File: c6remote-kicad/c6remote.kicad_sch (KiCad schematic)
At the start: 29 parts, among them J1 Battery, Q1 MMBT2222A, SW1 SW_Push, SW10 SW_Push, SW11 SW_Push, SW2 SW_Push, SW3 SW_Push, SW4 SW_Push, SW5 SW_Push, SW6 SW_Push, SW7 SW_Push, SW8 SW_Push, SW9 SW_Push, U1 XIAO-ESP32-C6, U2 TSOP4136, U3 PCF8575DBR

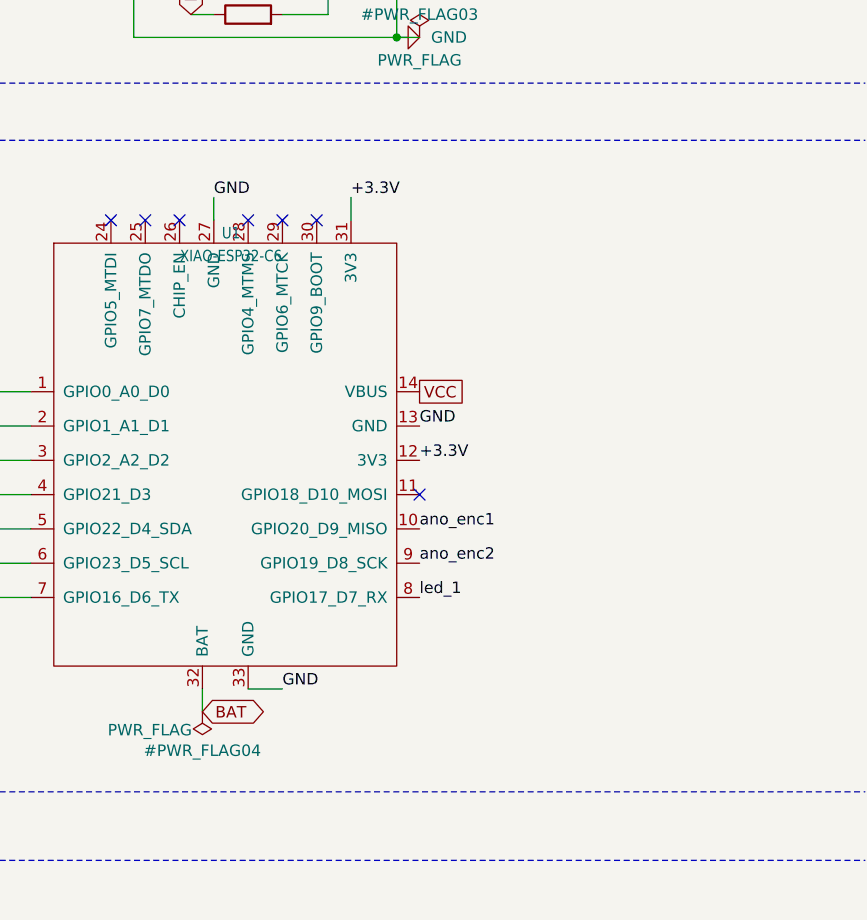
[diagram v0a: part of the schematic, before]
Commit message: feat(batt): add battery voltage-sense divider R7/R8 (100k/100k 0603) BAT->bat_sense->GND with midpoint to U1 GPIO4/pin28 ADC (halves 4.2V LiPo to ~2.1V for 3.3V ADC, ~21uA drain), routed on PCB w/ DRC 0 errors + 0 unconnected; regenerated export/ gerbers+drill+pos+BOM incl R7/R8; firmware reads ADC1 on GPIO4 as V_batt=V_adc*2. (sch/pcb reformatted by KiCad re-save, semantic delta is only the divider + routing)
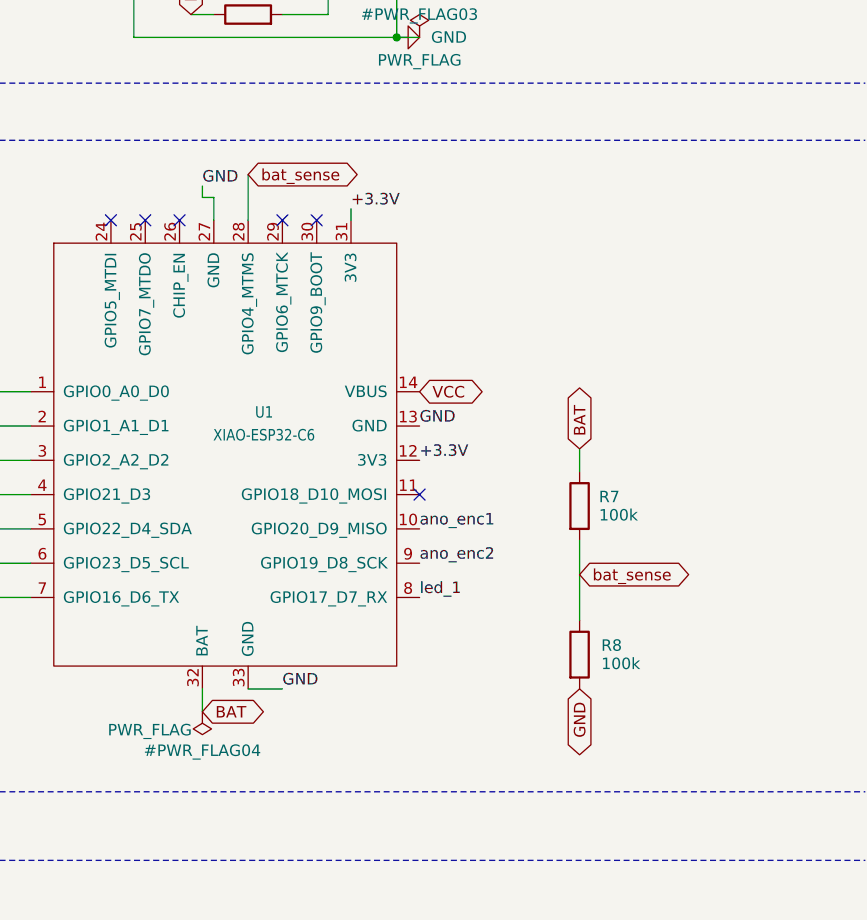
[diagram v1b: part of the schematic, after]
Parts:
- added R7, R8: 100k, Resistor_SMD:R_0603_1608Metric, symbol Device:R
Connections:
- net BAT: now also R7.1
- net GND: now also R8.2
- net bat_sense: now reaches U1.28 (GPIO4_MTMS)
- net bat_sense: now also R7.2, R8.1
- no-connect marks 9 -> 8

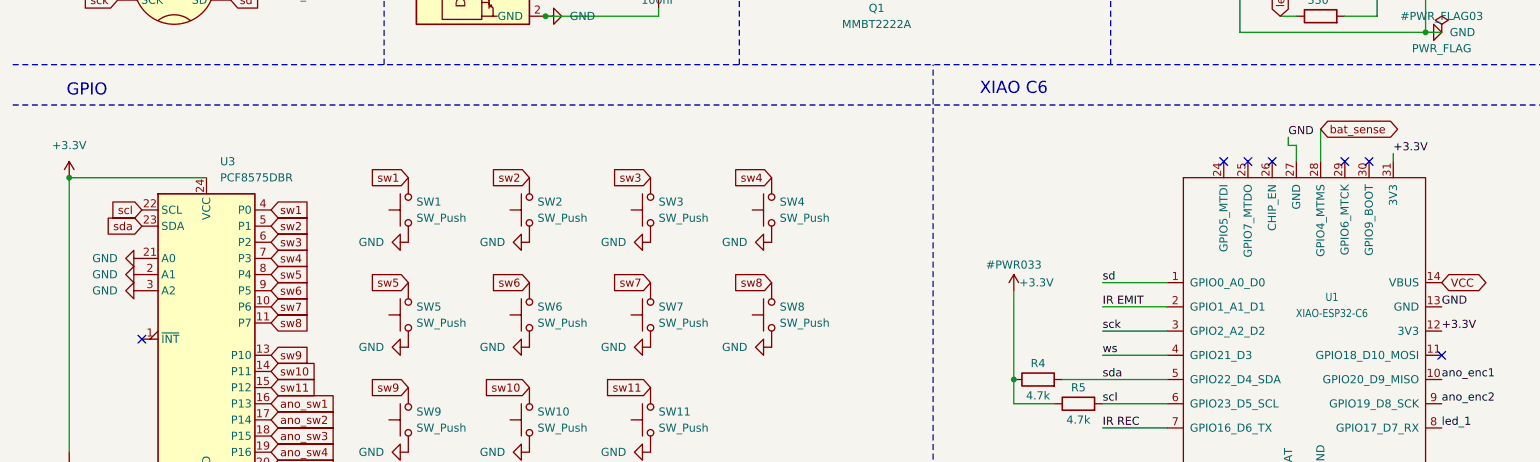
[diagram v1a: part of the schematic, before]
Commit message: feat(wake): add deep-sleep button wake via U3 PCF8575 ~INT -> new exp_int net to U1 GPIO5/pad24 (LP GPIO, ext1 wake) with R9 100k 0603 pullup to +3.3V next to R7/R8; schematic label + stale no-connect removed, board routed U3 pad1 down west channel x=48.25 w/ 2 vias joining existing GPIO5 trace at via (58.5,156.75); DRC 0 errors 0 unconnected (14 parity warns = pre-existing TP_*), no new ERC; regen export/ fab + readme renders; fw: esp_sleep_enable_ext1_wakeup(BIT(5), ANY_LOW) then read expander over I2C to identify button
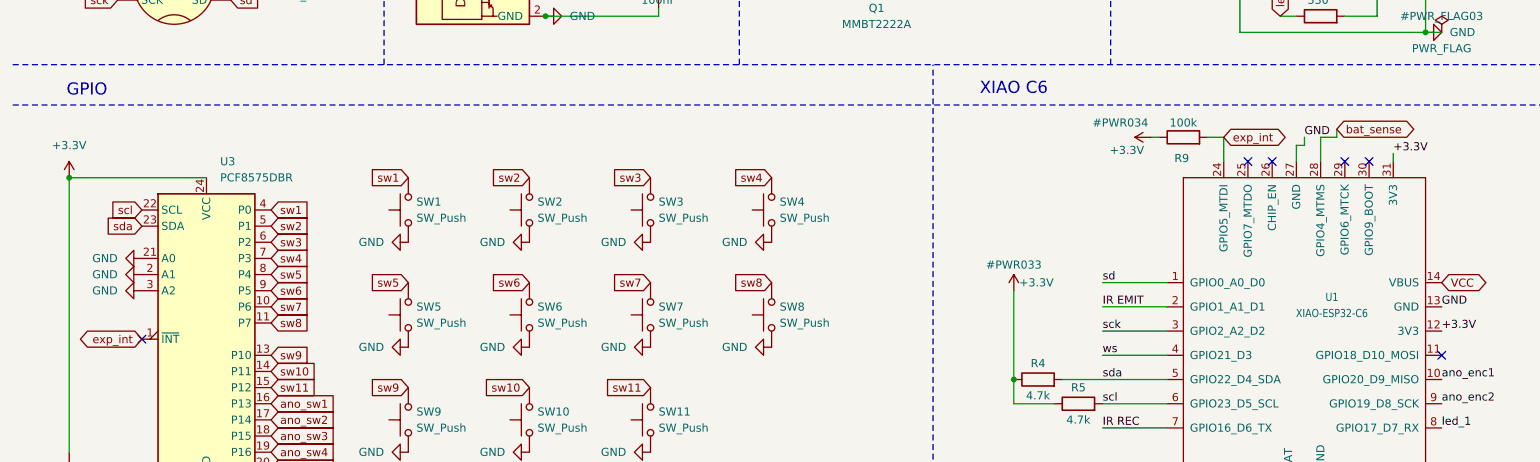
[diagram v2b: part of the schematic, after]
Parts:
- added R9: 100k, Resistor_SMD:R_0603_1608Metric, symbol Device:R
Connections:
- net +3.3V: now also R9.1
- net exp_int: now reaches U3.1 (~{INT})
- net exp_int: now also U1.24 (GPIO5_MTDI), R9.2
- no-connect marks 8 -> 7

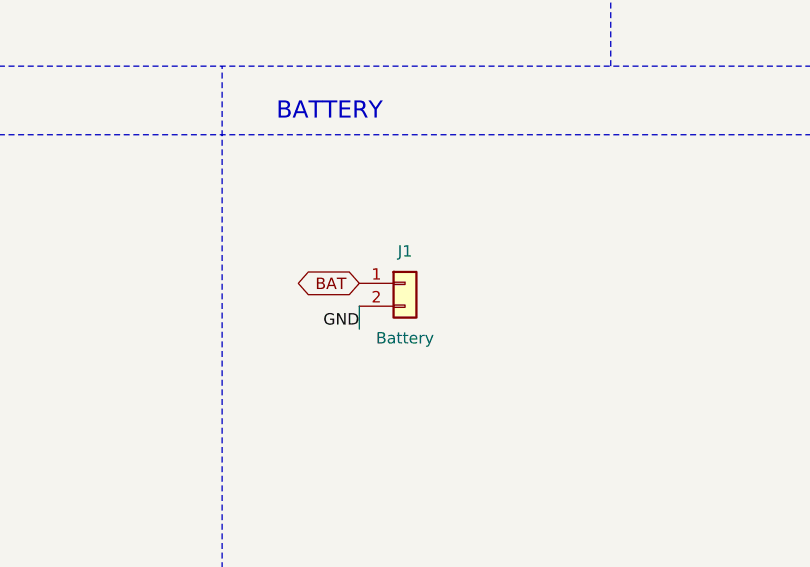
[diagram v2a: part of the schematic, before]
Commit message: fix(J1): replace battery connector footprint with real SMD JST S2B-PH-SM4-TB(LF)(SN) (1x02-1MP horizontal) — prior embedded footprint was THT S2B-PH-K name with hand-converted SMD pads and no drills (fab flagged missing PTHs; true THT impossible, holes would short U1 pads 24/25 on F.Cu above); pads 1/2 land on existing BAT/GND track ends (52.9/54.9,155.7), MP anchors face interior, wire entry toward board center; add JST MPN/Manufacturer/Description fields to schematic+board for BOM sourcing; ERC 14 warns + DRC 0 errors 0 unconnected 14 parity = unchanged baseline
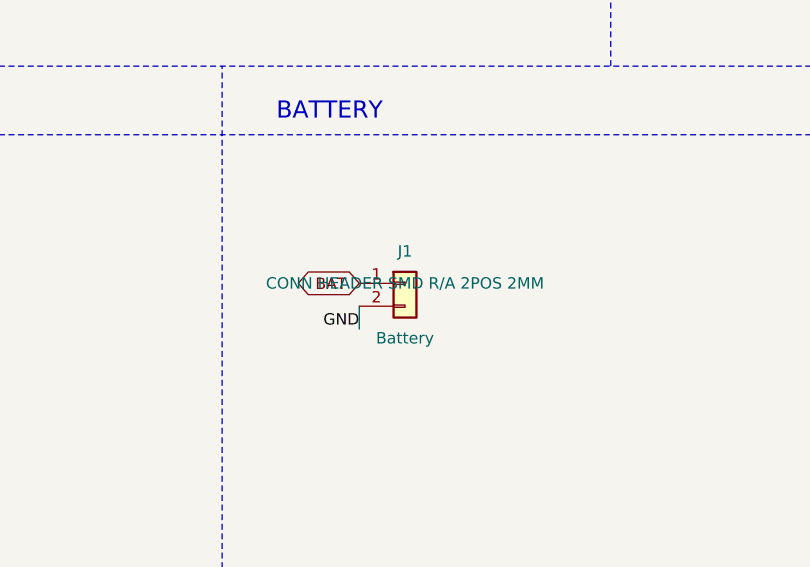
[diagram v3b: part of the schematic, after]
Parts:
- J1: footprint Connector_JST:JST_PH_S2B-PH-K_1x02_P2.00mm_Horizontal -> Connector_JST:JST_PH_S2B-PH-SM4-TB_1x02-1MP_P2.00mm_Horizontal; MPN (none) -> S2B-PH-SM4-TB(LF)(SN); Manufacturer (none) -> JST
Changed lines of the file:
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@@
 			)
 		)
-		(property "Footprint" "Connector_JST:JST_PH_S2B-PH-K_1x02_P2.00mm_Horizontal"
+		(property "Footprint" "Connector_JST:JST_PH_S2B-PH-SM4-TB_1x02-1MP_P2.00mm_Horizontal"
 			(at 133.35 153.67 0)
 			(hide yes)
@@
 			)
 		)
-		(property "Description" ""
+		(property "Description" "CONN HEADER SMD R/A 2POS 2MM"
 			(at 133.35 153.67 0)
 			(show_name no)
 			(do_not_autoplace no)
+			(effects
+				(font
+					(size 1.27 1.27)
+				)
+			)
+		)
+		(property "Manufacturer" "JST"
+			(at 133.35 153.67 0)
+			(hide yes)
+			(show_name no)
+			(do_not_autoplace no)
+			(effects
+				(font
+					(size 1.27 1.27)
+				)
+			)
+		)
+		(property "MPN" "S2B-PH-SM4-TB(LF)(SN)"
+			(at 133.35 153.67 0)
+			(hide yes)
+			(show_name no)
+			(do_not_autoplace no)
